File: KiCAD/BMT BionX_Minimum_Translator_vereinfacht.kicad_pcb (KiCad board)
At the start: 2 copper layers, 89.9 x 73.2 mm, 28 parts, among them J1 Kunteng LCDx Display Connector, J2 SAE Power Connector Motor, J3 Rosenberg Motor, J4 External BB Torquesensor, J5 Brake connector, J6 Throttle connector, J7 CAN Connector, J9 Batterieanschluß, Q1 IRF3205, Q2 IRF3205, U1 BP, U2 MCP2551-CAN Transceiver, U3 VOM1271, U4 SD12-5

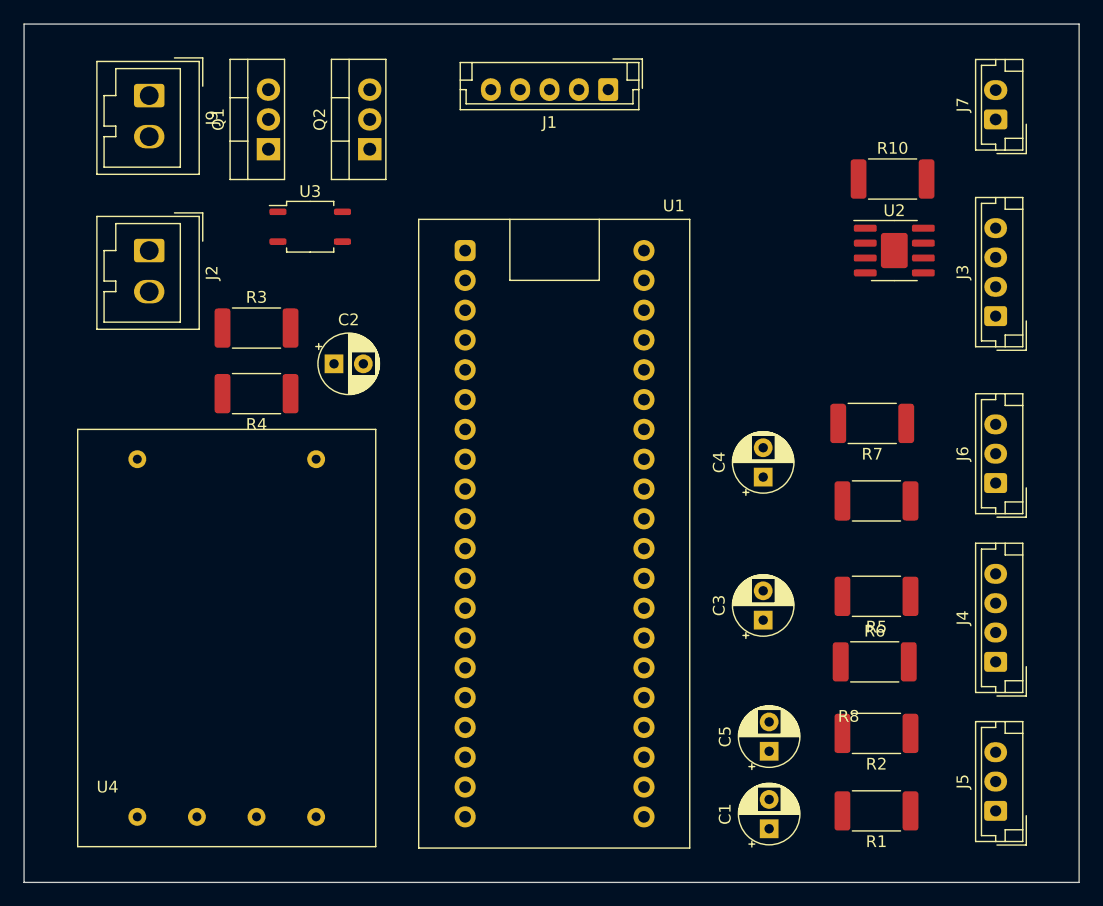
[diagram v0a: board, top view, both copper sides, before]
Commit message: switched to 0805 Size
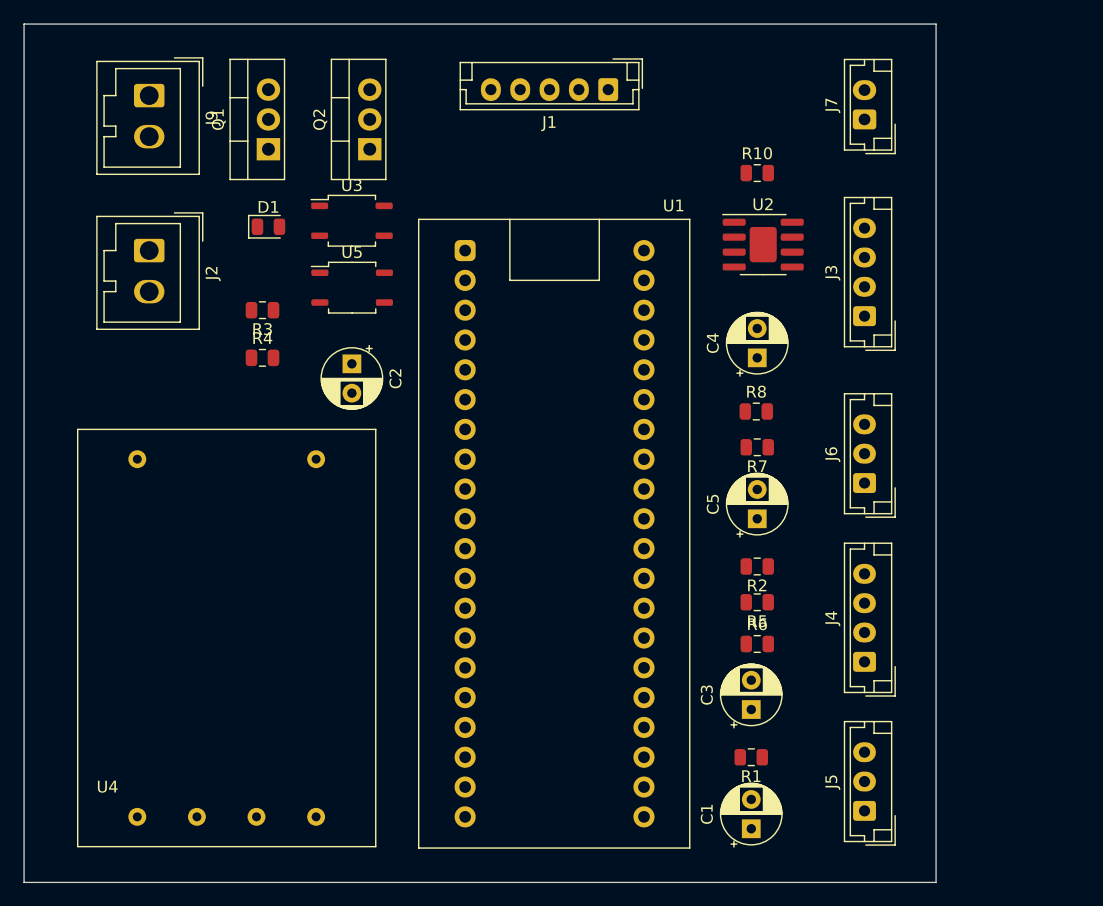
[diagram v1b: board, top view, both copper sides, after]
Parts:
- added D1: D_Zener, Diode_SMD:D_0805_2012Metric, F.Cu at (68.1, 73.7)
- added U5: VOM1271, Package_SO:SOP-4_3.8x4.1mm_P2.54mm, F.Cu at (75.2, 78.9)
- R1, R10, R2, R3, R4, R5, R6, R7, R8: footprint Resistor_SMD:R_2512_6332Metric -> Resistor_SMD:R_0805_2012Metric
- moved C5 19.8 mm to (109.7, 98.6)
- moved R2 17.5 mm to (109.7, 102.6)
- moved R8 12.8 mm to (109.6, 89.4)
- moved R1 11.6 mm to (109.2, 118.9)
- moved R10 11.5 mm to (109.7, 69.1)
- moved U2 11.2 mm to (110.2, 75.2)
- moved J3 11.2 mm to (118.9, 81.3)
- moved J4 11.2 mm to (118.9, 110.7)
- moved J5 11.2 mm to (118.9, 123.4)
- moved J6 11.2 mm to (118.9, 95.5)
- moved J7 11.2 mm to (118.9, 64.5)
- moved R5 10.2 mm to (109.7, 105.7)
- moved C4 10.2 mm to (109.7, 84.8)
- moved R6 10.1 mm to (109.7, 109.2)
- moved R7 10.0 mm to (109.7, 92.5)
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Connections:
- Q1 pad 1: Net-(Q1-Pad1) -> Net-(D1-Pad1)
- Q2 pad 1: Net-(Q1-Pad1) -> Net-(D1-Pad1)
- U3 pad 3: Net-(Q1-Pad1) -> Net-(U3-Pad3)
- U3 pad 4: Net-(Q1-Pad3) -> Net-(D1-Pad1)
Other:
- board size 89.9 x 73.2 mm -> 77.7 x 73.2 mm

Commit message: 2 Layer routing
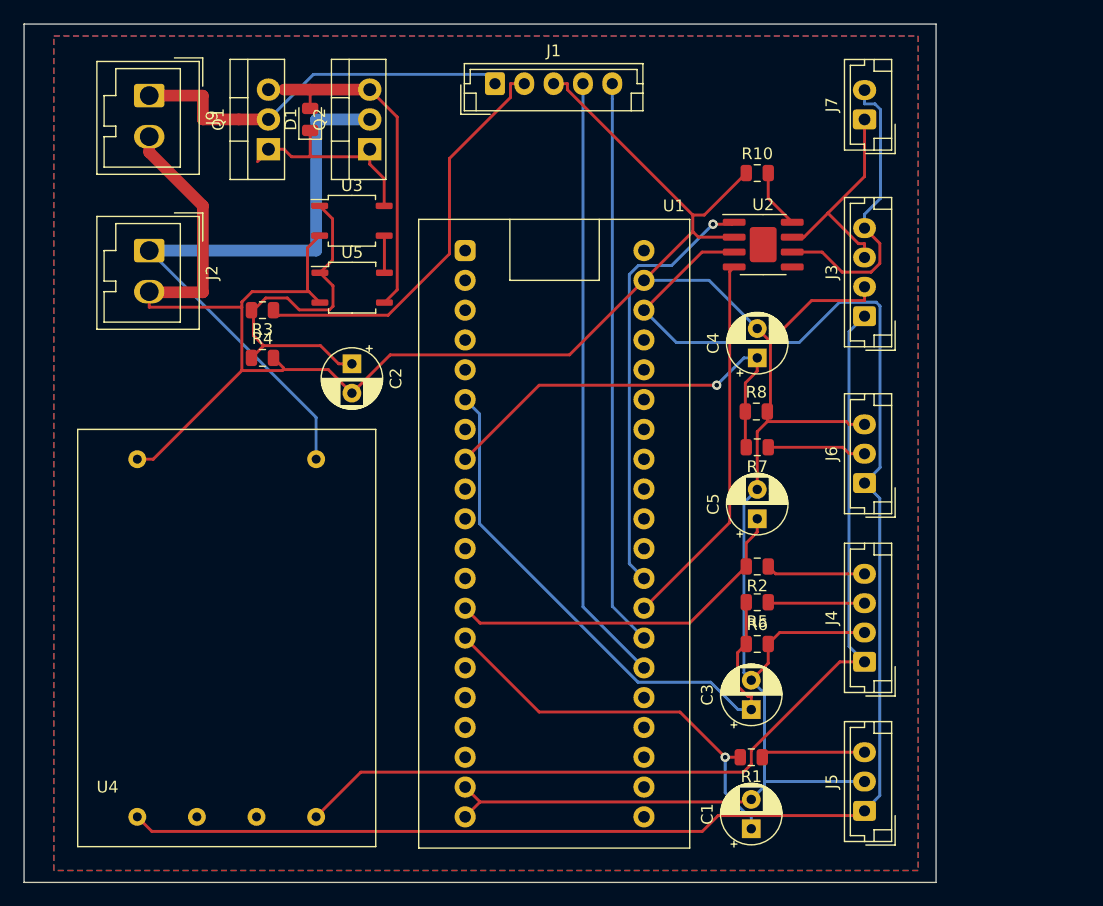
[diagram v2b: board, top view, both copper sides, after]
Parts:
- D1: value D_Zener -> 15V
- J1: value Kunteng LCDx Display Connector -> Kunteng Display Connector
- moved D1 9.81 mm to (71.6, 64.5), turned to 90 degrees
- moved J1 9.67 mm to (87.4, 61.5), turned to 0 degrees
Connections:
- D1 pad 2: +BATT -> Net-(D1-Pad2)
- J1 pad 1: Net-(J1-Pad1) -> +BATT
- J1 pad 2: GND -> Net-(J1-Pad2)
- J1 pad 3: +BATT -> GND
- Q1 pad 3: Net-(Q1-Pad3) -> Net-(D1-Pad2)
- Q2 pad 3: Net-(Q1-Pad3) -> Net-(D1-Pad2)
- R3 pad 1: Net-(J1-Pad4) -> Net-(J1-Pad2)
- U1 pad PA10: Net-(J1-Pad1) -> Net-(J1-Pad5)
- U1 pad PA9: Net-(J1-Pad5) -> Net-(J1-Pad4)
- U5 pad 3: Net-(Q1-Pad3) -> Net-(D1-Pad2)
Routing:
- net GND: track 0.00 -> 254.5 mm
- net Net-(J5-Pad1): track 0.00 -> 140.4 mm
- net Net-(J3-Pad1): track 0.00 -> 83.5 mm
- net Net-(J2-Pad1): track 0.00 -> 53.6 mm
- net Net-(J1-Pad4): track 0.00 -> 51.9 mm
- net Net-(C3-Pad1): track 0.00 -> 50.9 mm
- net Net-(J1-Pad5): track 0.00 -> 48.4 mm
- net Net-(U1-PadPA12): track 0.00 -> 37.2 mm, vias 0 -> 1
- net Net-(C4-Pad1): track 0.00 -> 36.5 mm, vias 0 -> 1
- net Net-(J1-Pad2): track 0.00 -> 35.2 mm
- net Net-(C1-Pad1): track 0.00 -> 34.8 mm, vias 0 -> 1
- net +BATT: track 0.00 -> 33.4 mm
- net Net-(U1-PadPA11): track 0.00 -> 32.3 mm
- net Net-(C5-Pad1): track 0.00 -> 30.9 mm
- net Net-(C2-Pad1): track 0.00 -> 30.9 mm
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- added copper zone on B.Cu, net GND
- added copper zone on F.Cu, net GND

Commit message: Step Down switched seperately
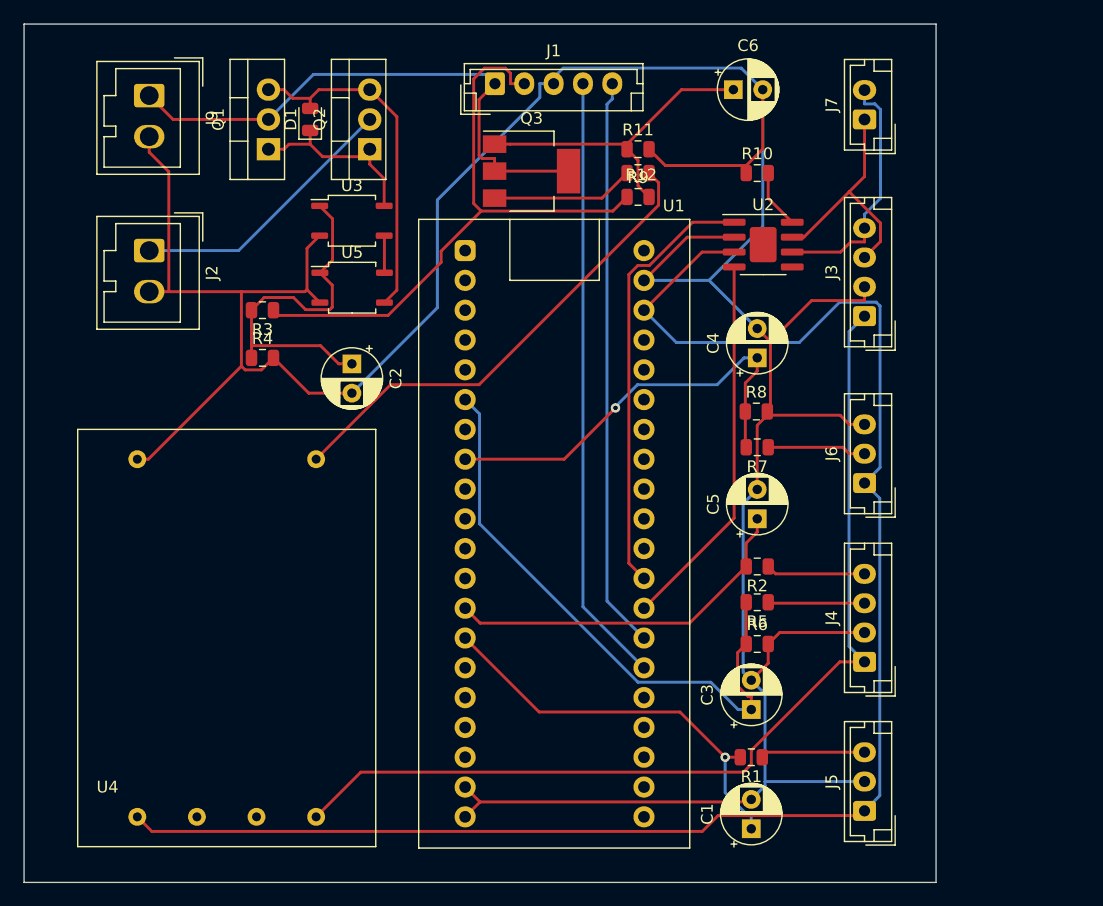
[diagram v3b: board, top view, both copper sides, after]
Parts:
- added C6: 10µ, Capacitor_THT:CP_Radial_D5.0mm_P2.50mm, F.Cu at (107.7, 62.0)
- added Q3: BCP56, Package_TO_SOT_SMD:SOT-223, F.Cu at (90.5, 68.9)
- added R11: 2.2k, Resistor_SMD:R_0805_2012Metric, F.Cu at (99.6, 67.1)
- added R12: 22, Resistor_SMD:R_0805_2012Metric, F.Cu at (99.6, 69.1)
- added R9: 1k, Resistor_SMD:R_0805_2012Metric, F.Cu at (99.6, 71.1)
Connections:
- U4 pad V_in: Net-(J2-Pad1) -> Net-(R12-Pad2)
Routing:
- net Net-(R12-Pad2): track 0.00 -> 41.2 mm
- net Net-(J2-Pad1): track 53.6 -> 23.4 mm
- net GND: track 254.5 -> 282.5 mm
- net Net-(C6-Pad1): track 0.00 -> 27.5 mm
- net Net-(J1-Pad2): track 35.2 -> 52.3 mm
- net +BATT: track 33.4 -> 47.7 mm
- net Net-(Q3-Pad3): track 0.00 -> 12.2 mm
- net Net-(J3-Pad4): track 25.4 -> 21.1 mm
- net Net-(D1-Pad1): track 18.0 -> 15.8 mm
- net Net-(J3-Pad3): track 18.5 -> 20.4 mm
- net Net-(U1-PadPA12): track 37.2 -> 37.3 mm, vias 1 -> 0
- removed copper zone on B.Cu, net GND
- removed copper zone on F.Cu, net GND

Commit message: separated voltage regulators as alternative added.
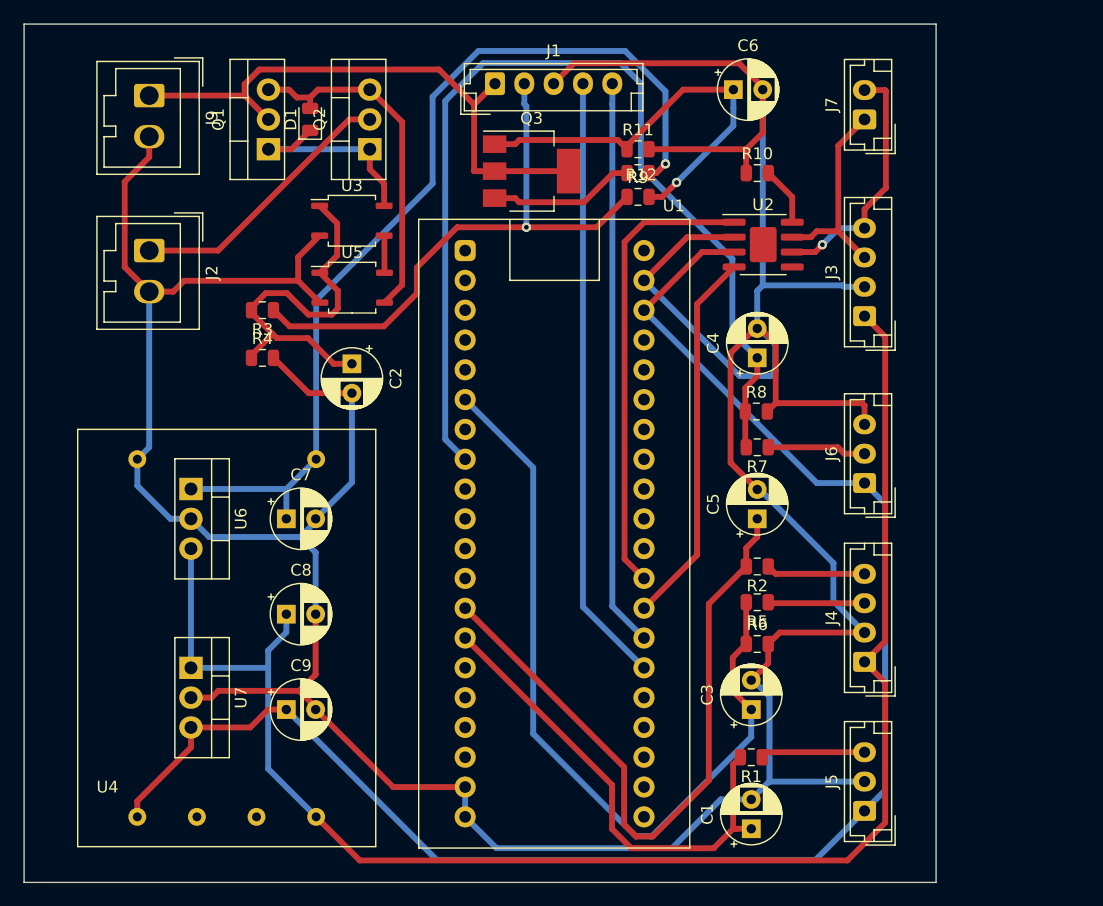
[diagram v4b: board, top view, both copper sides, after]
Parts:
- added C7: 10µ, Capacitor_THT:CP_Radial_D5.0mm_P2.50mm, F.Cu at (69.6, 98.6)
- added C8: 10µ, Capacitor_THT:CP_Radial_D5.0mm_P2.50mm, F.Cu at (69.6, 106.7)
- added C9: 10µ, Capacitor_THT:CP_Radial_D5.0mm_P2.50mm, F.Cu at (69.6, 114.8)
- added U6: LM7812_TO220, Package_TO_SOT_THT:TO-220-3_Vertical, F.Cu at (61.5, 96.0)
- added U7: LM7805_TO220, Package_TO_SOT_THT:TO-220-3_Vertical, F.Cu at (61.5, 111.3)
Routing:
- net GND: track 282.5 -> 335.4 mm
- net Net-(C8-Pad1): track 83.5 -> 133.1 mm
- net Net-(C4-Pad1): track 36.6 -> 85.5 mm, vias 1 -> 0
- net Net-(C7-Pad1): track 41.2 -> 80.0 mm, vias 0 -> 1
- net Net-(C5-Pad1): track 30.9 -> 57.7 mm
- net Net-(C3-Pad1): track 50.9 -> 69.2 mm
- net Net-(C6-Pad1): track 27.5 -> 35.8 mm, vias 0 -> 1
- net Net-(C1-Pad1): track 34.8 -> 41.0 mm, vias 1 -> 0
- net Net-(J1-Pad2): track 52.3 -> 48.9 mm, vias 0 -> 1
- net Net-(J3-Pad3): track 20.4 -> 17.8 mm
- net Net-(D1-Pad1): track 15.8 -> 18.2 mm
- net Net-(U1-PadPA12): track 37.3 -> 39.4 mm
- net Net-(C2-Pad1): track 31.1 -> 33.1 mm
- net Net-(C9-Pad1): track 140.4 -> 138.6 mm
- net +BATT: track 47.7 -> 49.5 mm
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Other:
- net class Default: clearance 0.2 -> 0.5; trace_width 0.25 -> 0.5
- rule trace_clearance: 0.2 -> 0.5
